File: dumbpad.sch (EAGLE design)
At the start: 42 parts

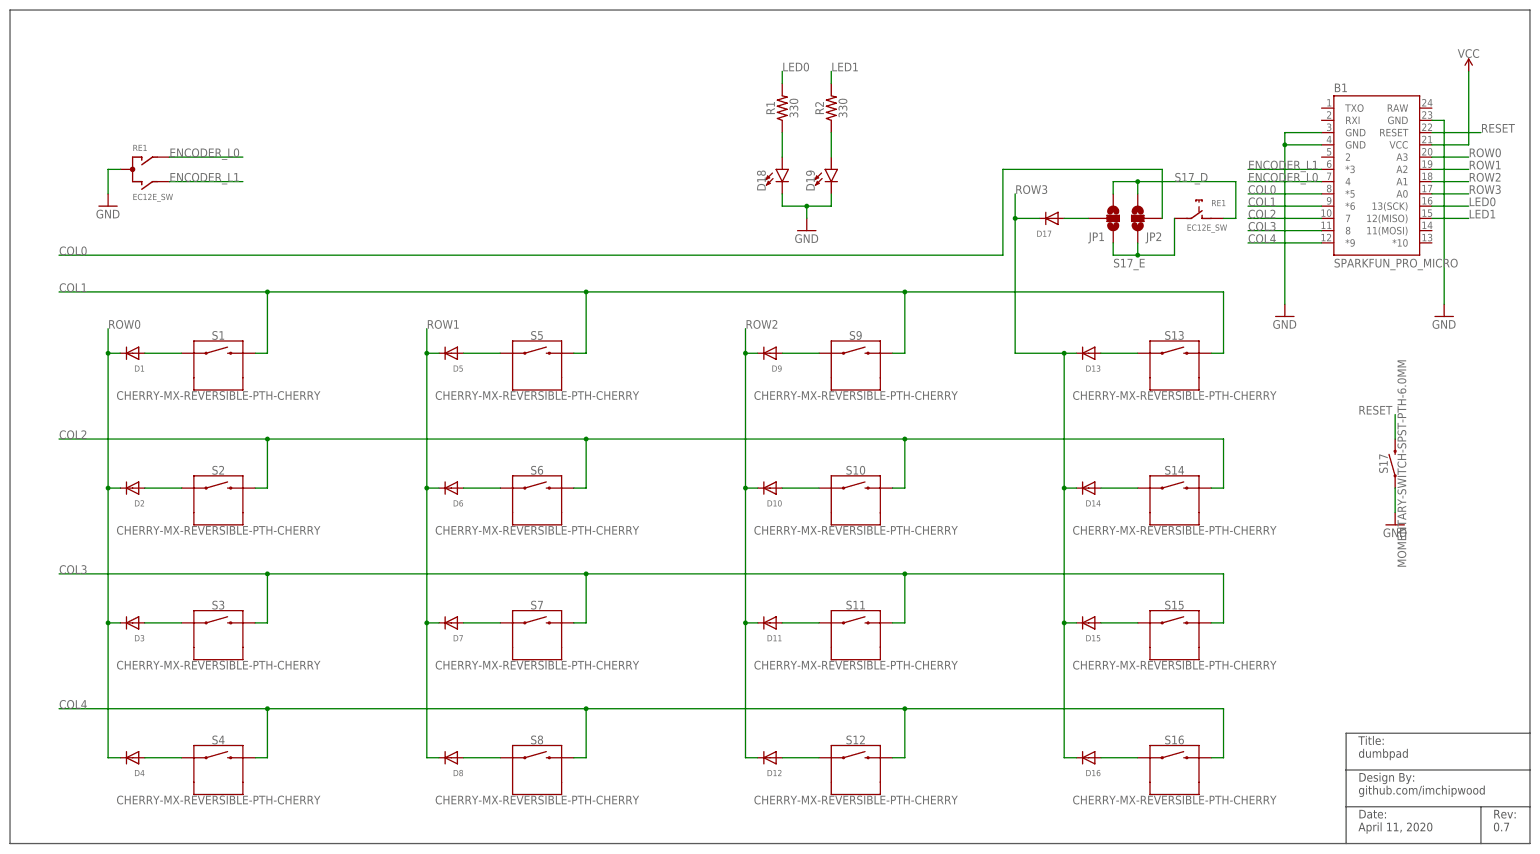
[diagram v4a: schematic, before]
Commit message: added 3rd LED for numlock indication
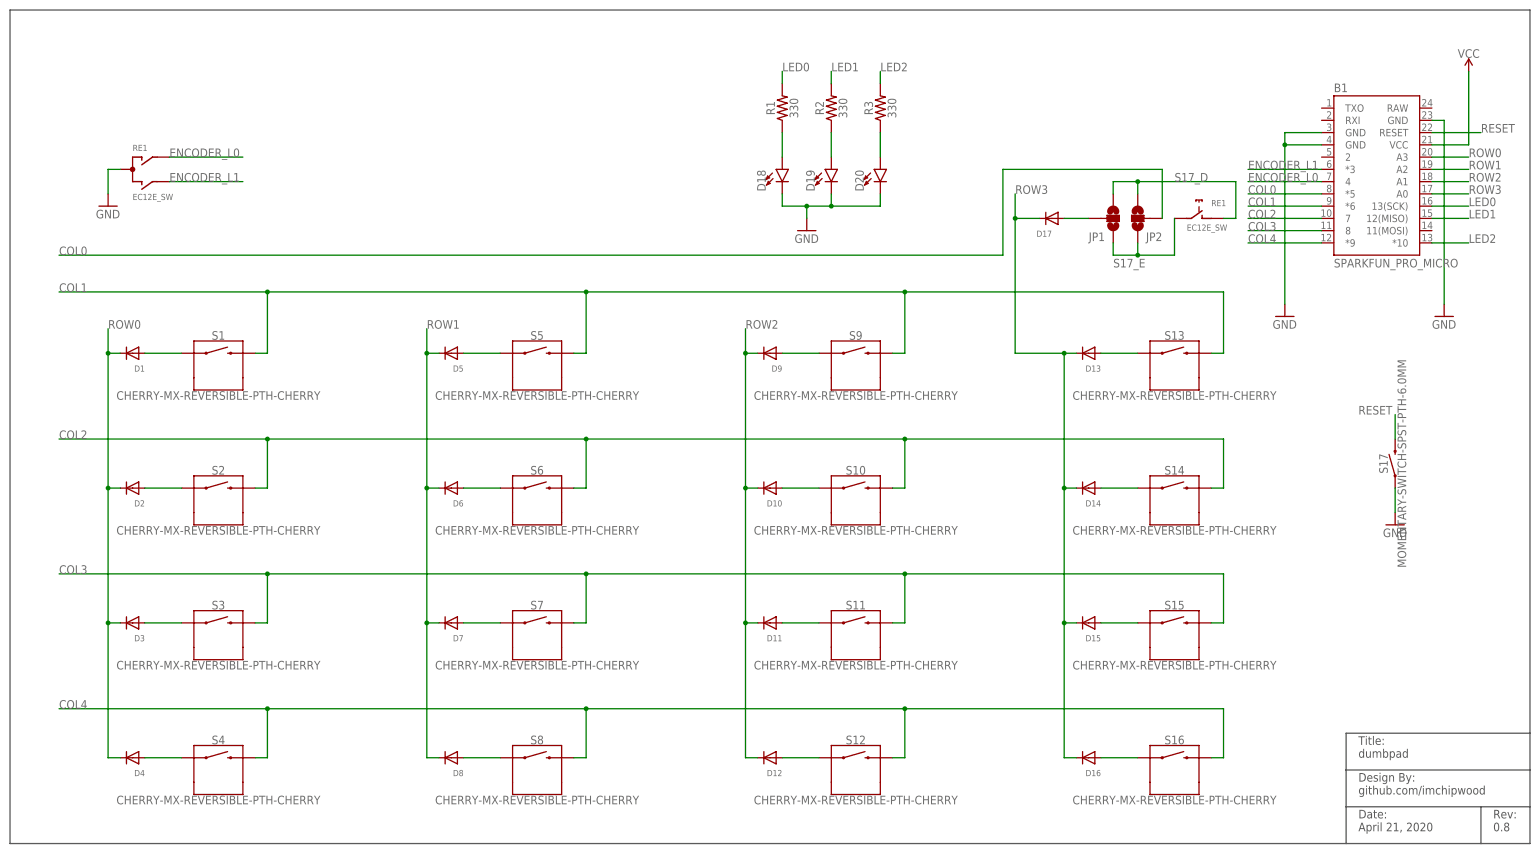
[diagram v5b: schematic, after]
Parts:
- added D20: (no value), SparkFun-LED:LED3MM
- added R3: 330, SparkFun-Resistors:330OHM-HORIZ-1/10W-5%
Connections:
- new net LED2: B1.*10, R3.2
- new net N$10: D20.A, R3.1
- net GND: now also D20.C
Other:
- note added: "Date: April 21, 2020"
- note added: "Rev: 0.8"
- note removed: "Date: April 11, 2020"
- note removed: "Rev: 0.7"
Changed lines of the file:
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@@
 <part name="JP1" library="SparkFun-Jumpers" deviceset="JUMPER-SMT_3_NO" device="_NO-SILK"/>
 <part name="JP2" library="SparkFun-Jumpers" deviceset="JUMPER-SMT_3_NO" device="_NO-SILK"/>
+<part name="D20" library="SparkFun-LED" deviceset="LED" device="3MM"/>
+<part name="R3" library="SparkFun-Resistors" deviceset="330OHM" device="-HORIZ-1/10W-5%" value="330"/>
 </parts>
 <sheets>
@@
 <wire x1="0" y1="172.72" x2="0" y2="0" width="0.1524" layer="97"/>
 <text x="307.34" y="2.54" size="1.778" layer="97">Rev:
-0.7</text>
+0.8</text>
 <text x="279.4" y="2.54" size="1.778" layer="97">Date:
-April 11, 2020</text>
+April 21, 2020</text>
 <text x="279.4" y="10.16" size="1.778" layer="97">Design By:
 github.com/imchipwood</text>
@@
 <attribute name="NAME" x="238.76" y="126.619" size="1.778" layer="95" font="vector" rot="R180"/>
 </instance>
+<instance part="D20" gate="D1" x="180.34" y="139.7" smashed="yes">
+<attribute name="NAME" x="176.911" y="135.128" size="1.778" layer="95" font="vector" rot="R90"/>
+<attribute name="VALUE" x="182.245" y="135.128" size="1.778" layer="96" font="vector" rot="R90" align="top-left"/>
+</instance>
+<instance part="R3" gate="G$1" x="180.34" y="152.4" smashed="yes" rot="R90">
+<attribute name="NAME" x="178.816" y="152.4" size="1.778" layer="95" font="vector" rot="R90" align="bottom-center"/>
+<attribute name="VALUE" x="181.864" y="152.4" size="1.778" layer="96" font="vector" rot="R90" align="top-center"/>
+</instance>
 </instances>
 <busses>
@@
 <pinref part="D19" gate="D1" pin="C"/>
 <wire x1="170.18" y1="132.08" x2="170.18" y2="134.62" width="0.1524" layer="91"/>
+<wire x1="170.18" y1="132.08" x2="180.34" y2="132.08" width="0.1524" layer="91"/>
+<junction x="170.18" y="132.08"/>
+<pinref part="D20" gate="D1" pin="C"/>
+<wire x1="180.34" y1="132.08" x2="180.34" y2="134.62" width="0.1524" layer="91"/>
 </segment>
 <segment>
@@
 </segment>
 </net>
+<net name="LED2" class="0">
+<segment>
+<pinref part="B1" gate="G$1" pin="*10"/>
+<wire x1="294.64" y1="124.46" x2="302.26" y2="124.46" width="0.1524" layer="91"/>
+<label x="302.26" y="124.46" size="1.778" layer="95"/>
+</segment>
+<segment>
+<pinref part="R3" gate="G$1" pin="2"/>
+<wire x1="180.34" y1="157.48" x2="180.34" y2="160.02" width="0.1524" layer="91"/>
+<label x="180.34" y="160.02" size="1.778" layer="95"/>
+</segment>
+</net>
+<net name="N$10" class="0">
+<segment>
+<pinref part="D20" gate="D1" pin="A"/>
+<pinref part="R3" gate="G$1" pin="1"/>
+<wire x1="180.34" y1="142.24" x2="180.34" y2="147.32" width="0.1524" layer="91"/>
+</segment>
+</net>
